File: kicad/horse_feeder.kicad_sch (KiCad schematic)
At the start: 0 parts

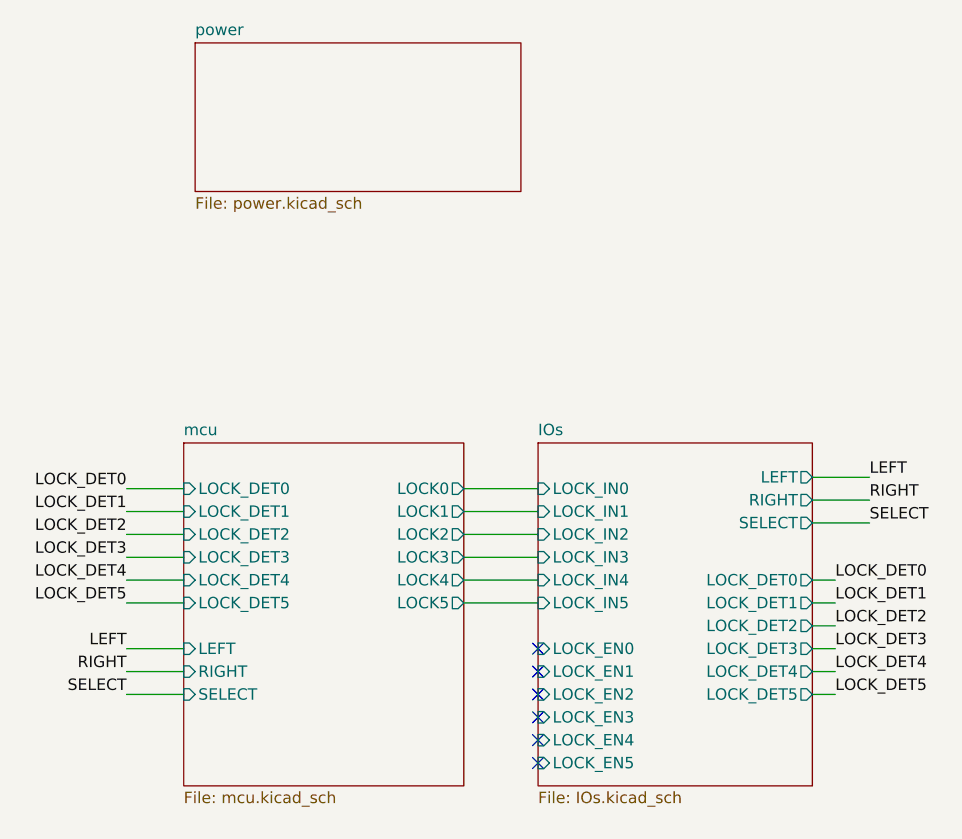
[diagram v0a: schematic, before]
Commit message: Update PCB with IO expander
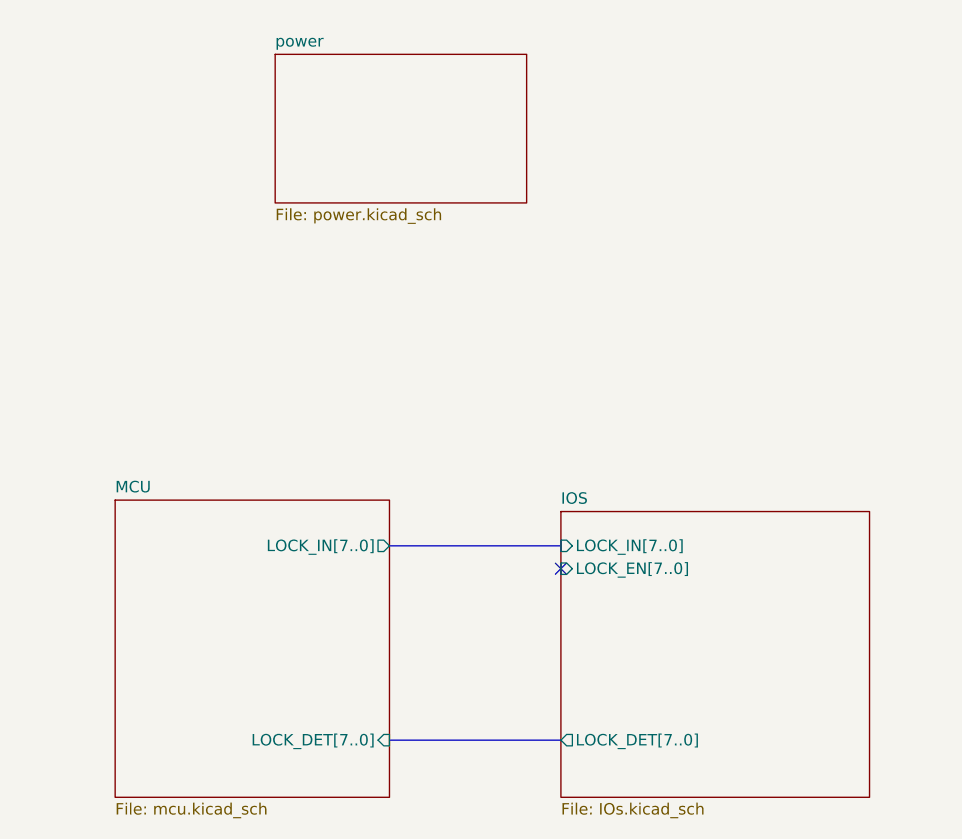
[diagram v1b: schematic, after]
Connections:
- no-connect marks 6 -> 1
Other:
- removed sheet IOs
- removed sheet mcu
- added sheet IOS (IOs.kicad_sch)
- added sheet MCU (mcu.kicad_sch)
